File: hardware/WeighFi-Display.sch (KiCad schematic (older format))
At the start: 43 parts, among them P1 CONN_12, P10 CONN_4, P11 CONN_1, P12 CONN_1, P13 CONN_1, P14 CONN_1, P15 CONN_1, P16 CONN_1, P17 CONN_1, P18 CONN_1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

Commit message: Refine schematics, generate new netlists
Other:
- moved on the sheet: C1, C2, C3, H1, H2, H3, H4, H5, H6, H7, P1, P10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

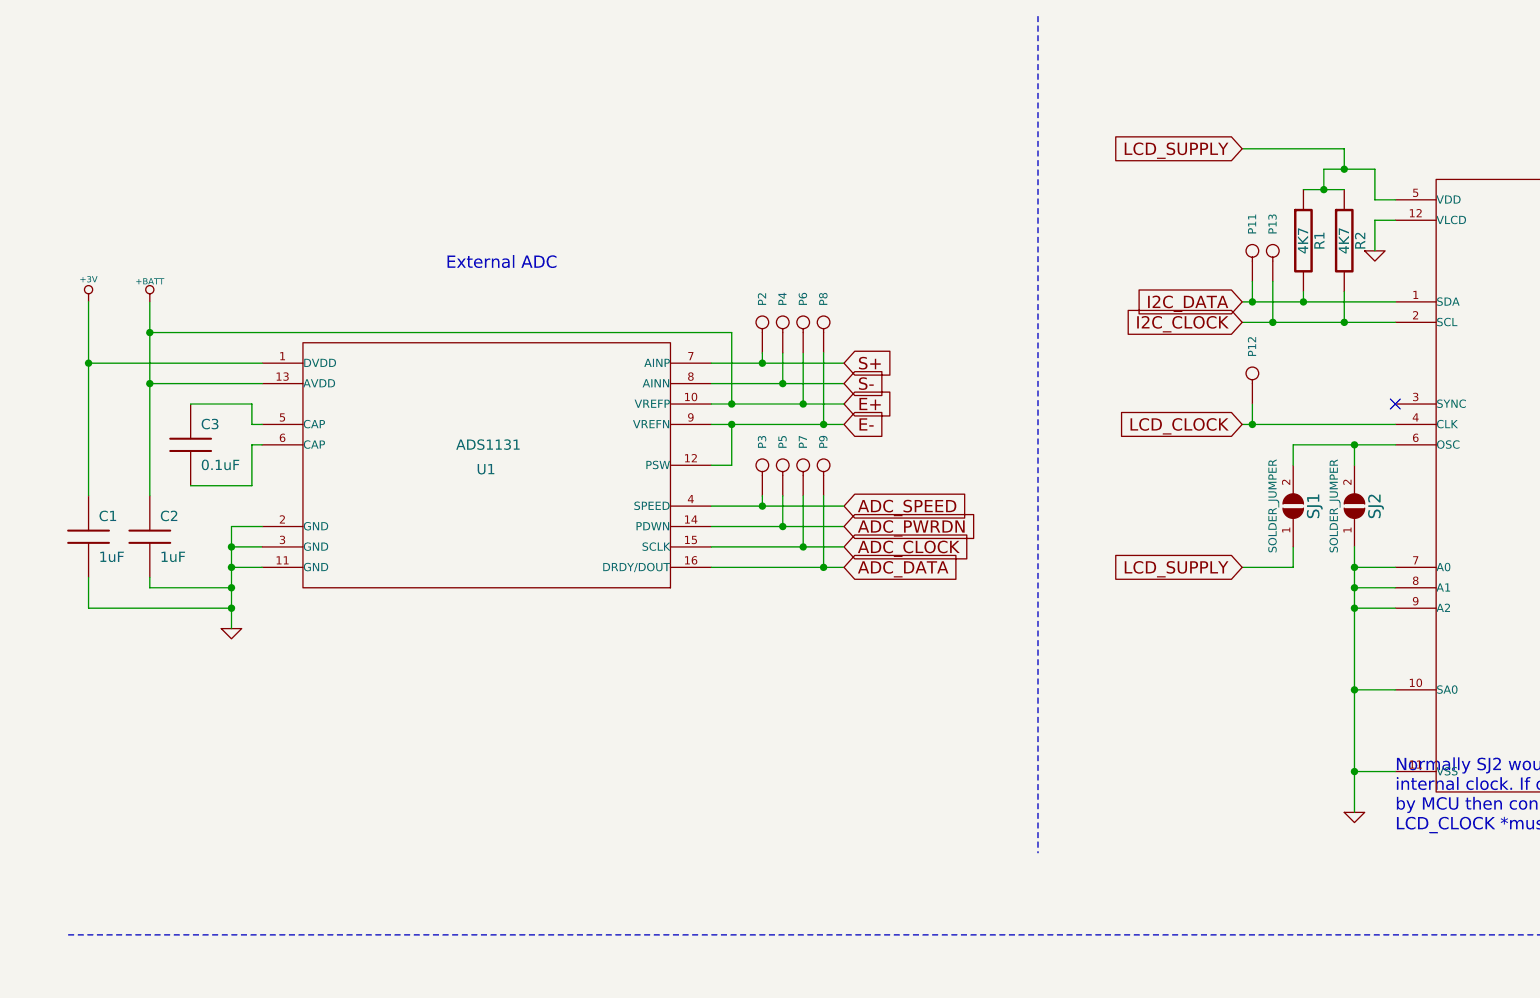
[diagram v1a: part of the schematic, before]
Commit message: Add decoupling capacitor for LCD driver IC
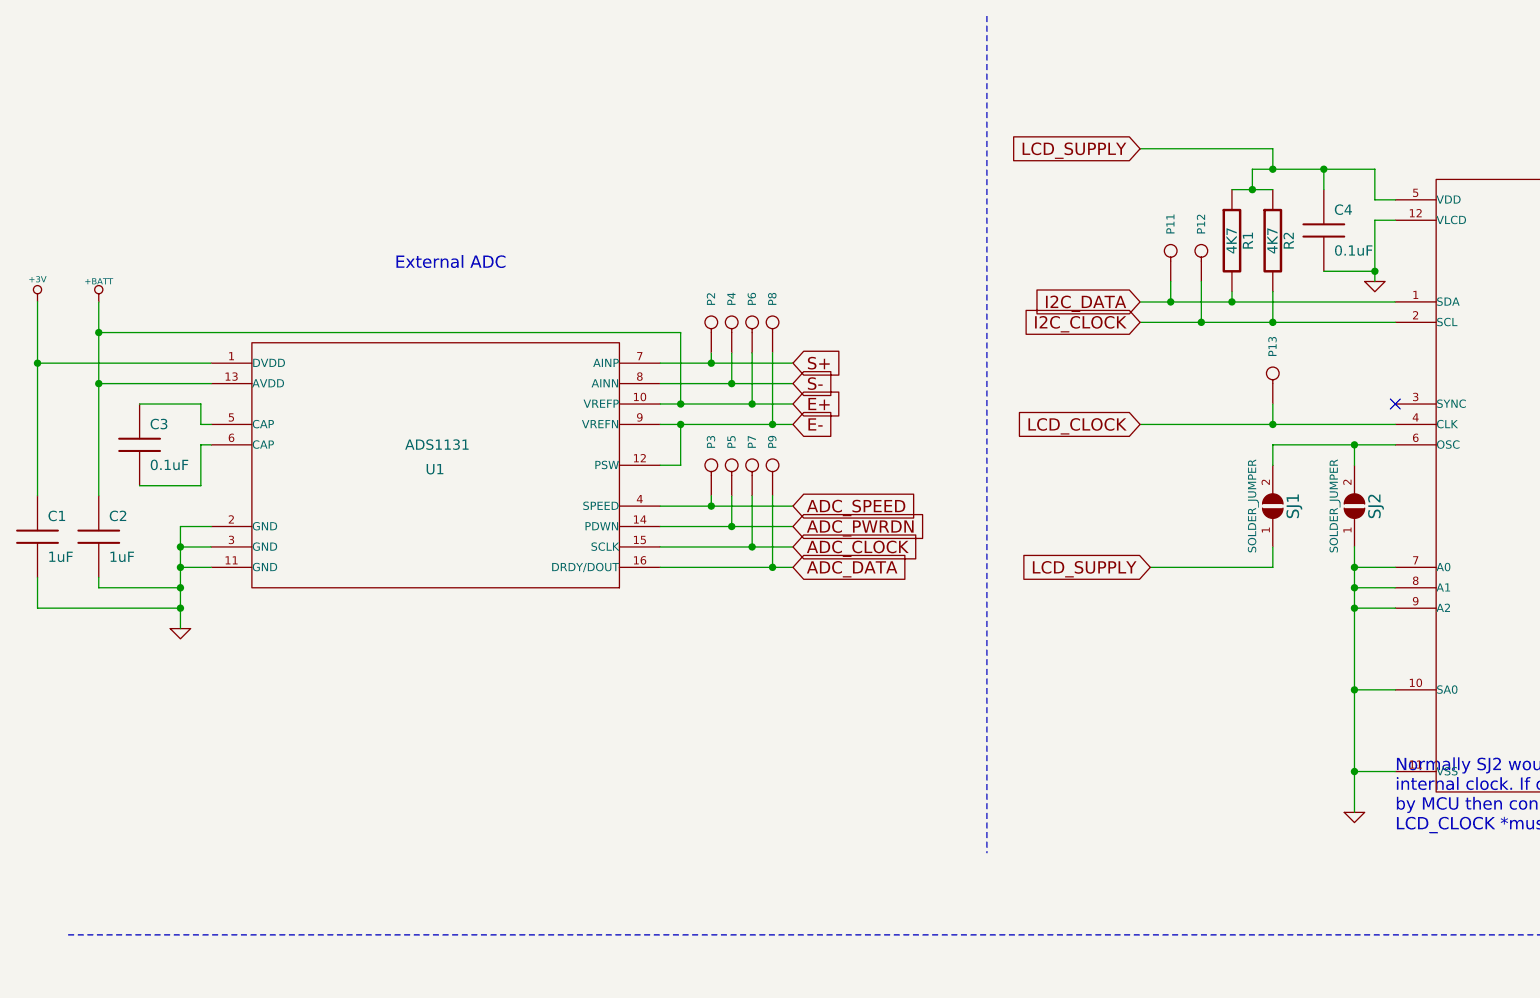
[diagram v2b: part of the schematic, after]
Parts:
- added C4: 0.1uF, symbol C
- renumbered P13 to P12, P12 to P13
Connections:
- net GND: now also C4.2
- net LCD_SUPPLY: now also C4.1
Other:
- moved on the sheet: C1, C2, C3, P11, P12, P13, P2, P3, P4, P5, P6, P7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

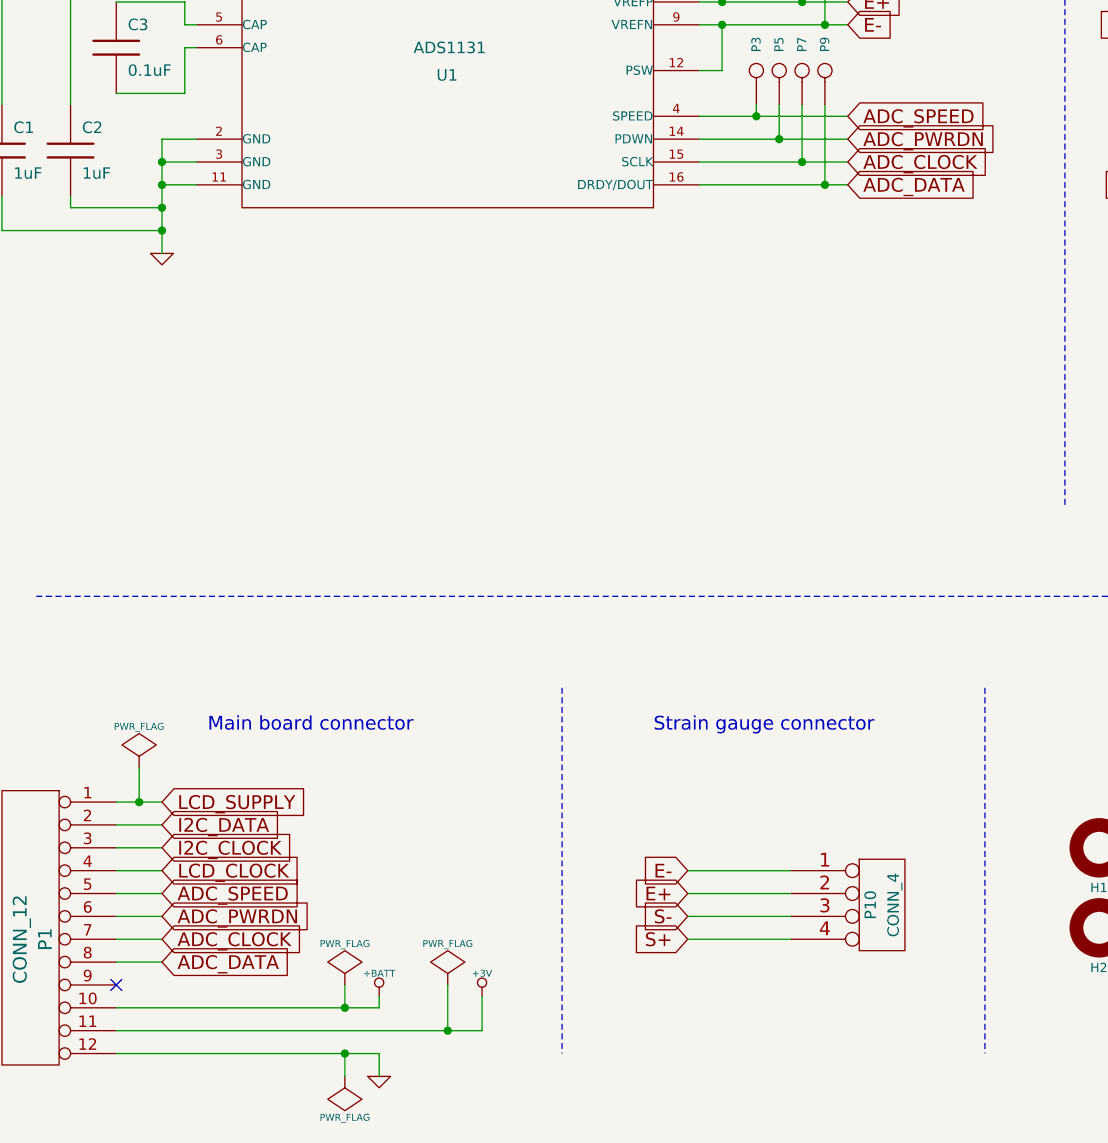
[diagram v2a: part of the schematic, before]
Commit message: Strain gauge daughter-board pinout changes between different revisions/models of the 'donor' scales. Add an alternate connector to accomodate either pinout.
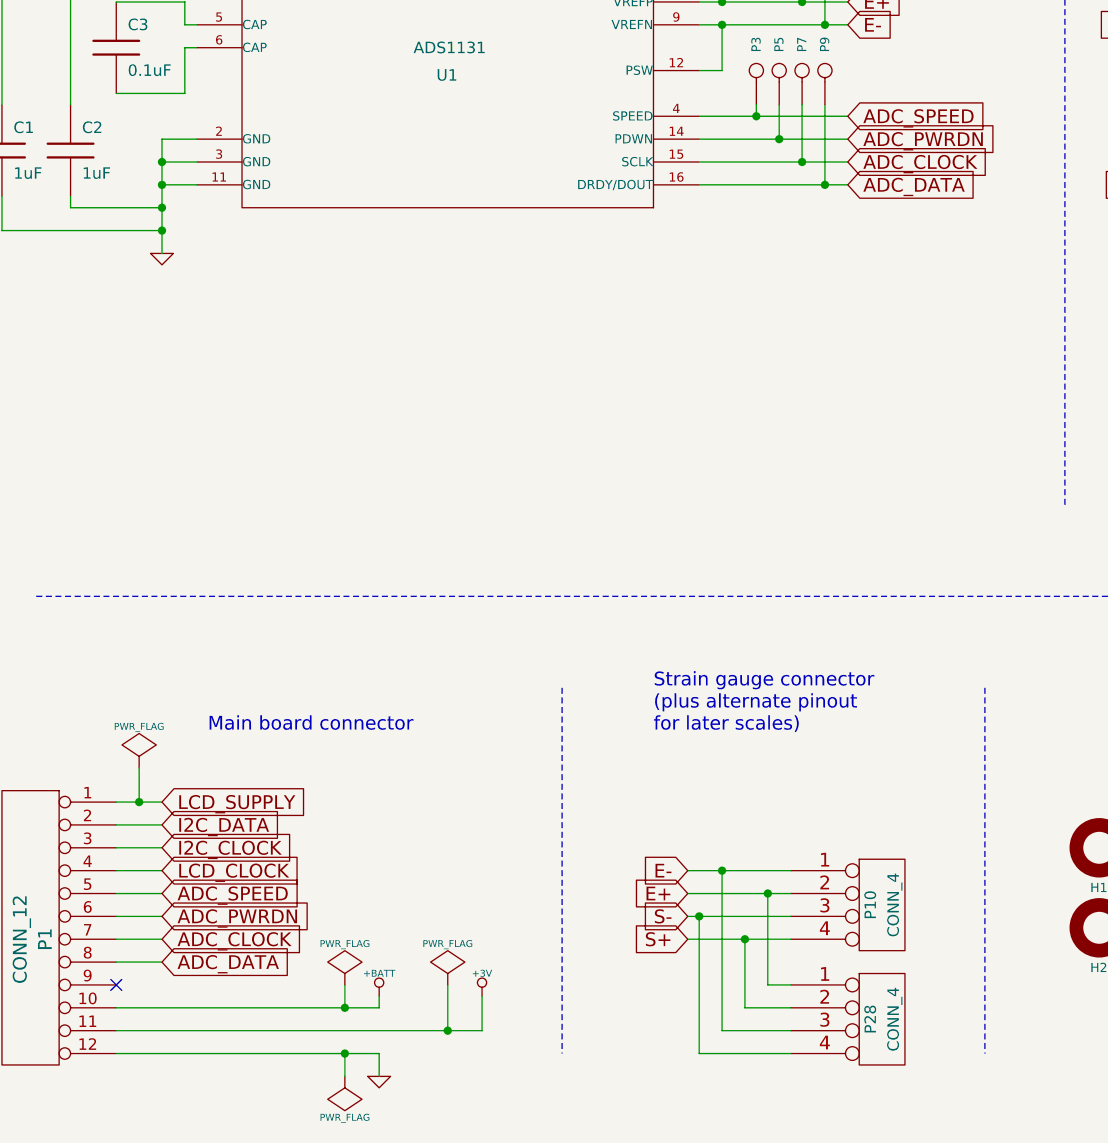
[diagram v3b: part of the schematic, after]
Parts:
- added P28: CONN_4, symbol CONN_4
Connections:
- net +BATT: now also P28.1
- net E-: now also P28.3
- net S+: now also P28.2
- net S-: now also P28.4
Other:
- note added: "Strain gauge connector\n(plus alternate pinout \nfor later scales)"
- note removed: "Strain gauge connector"
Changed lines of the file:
@@
-EESchema Schematic File Version 2  date Thu 06 Dec 2012 14:46:45 GMT
+EESchema Schematic File Version 2  date Mon 10 Dec 2012 10:51:47 GMT
 LIBS:dresco
 LIBS:WeighFi-Display-cache
@@
 Sheet 1 1
 Title "WeighFi-Display"
-Date "6 dec 2012"
+Date "10 dec 2012"
 Rev "1.0"
 Comp ""
@@
 Comment4 ""
 $EndDescr
+Connection ~ 3850 6700
+Wire Wire Line
+	3850 6700 3850 7300
+Wire Wire Line
+	3850 7300 4250 7300
+Connection ~ 4050 6800
+Wire Wire Line
+	4050 6800 4050 7100
+Wire Wire Line
+	4050 7100 4250 7100
 Connection ~ 7350 2050
 Wire Wire Line
@@
 Connection ~ 1500 3400
 Wire Wire Line
-	1500 3400 1650 3400
+	1650 3400 1500 3400
 Connection ~ 7250 4500
 Wire Wire Line
@@
 	7100 1550 7100 1650
 Connection ~ 7100 1550
+Wire Wire Line
+	4250 7000 4150 7000
+Wire Wire Line
+	4150 7000 4150 6600
+Connection ~ 4150 6600
+Wire Wire Line
+	4250 7200 3950 7200
+Wire Wire Line
+	3950 7200 3950 6500
+Connection ~ 3950 6500
+$Comp
+L CONN_4 P28
+U 1 1 50C5BDF5
+P 4650 7100
+F 0 "P28" V 4600 7050 50  0000 C CNN
+F 1 "CONN_4" V 4700 7050 50  0000 C CNN
+	1    4650 7100
+	1    0    0    -1
+$EndComp
 $Comp
 L C C4
@@
 $EndComp
 Text Notes 3650 5900 0    60   ~ 0
-Strain gauge connector
+Strain gauge connector\n(plus alternate pinout \nfor later scales)
 Text Notes 8300 1000 0    60   ~ 0
 LCD Driver
